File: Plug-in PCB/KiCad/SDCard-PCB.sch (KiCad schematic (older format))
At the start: 0 parts

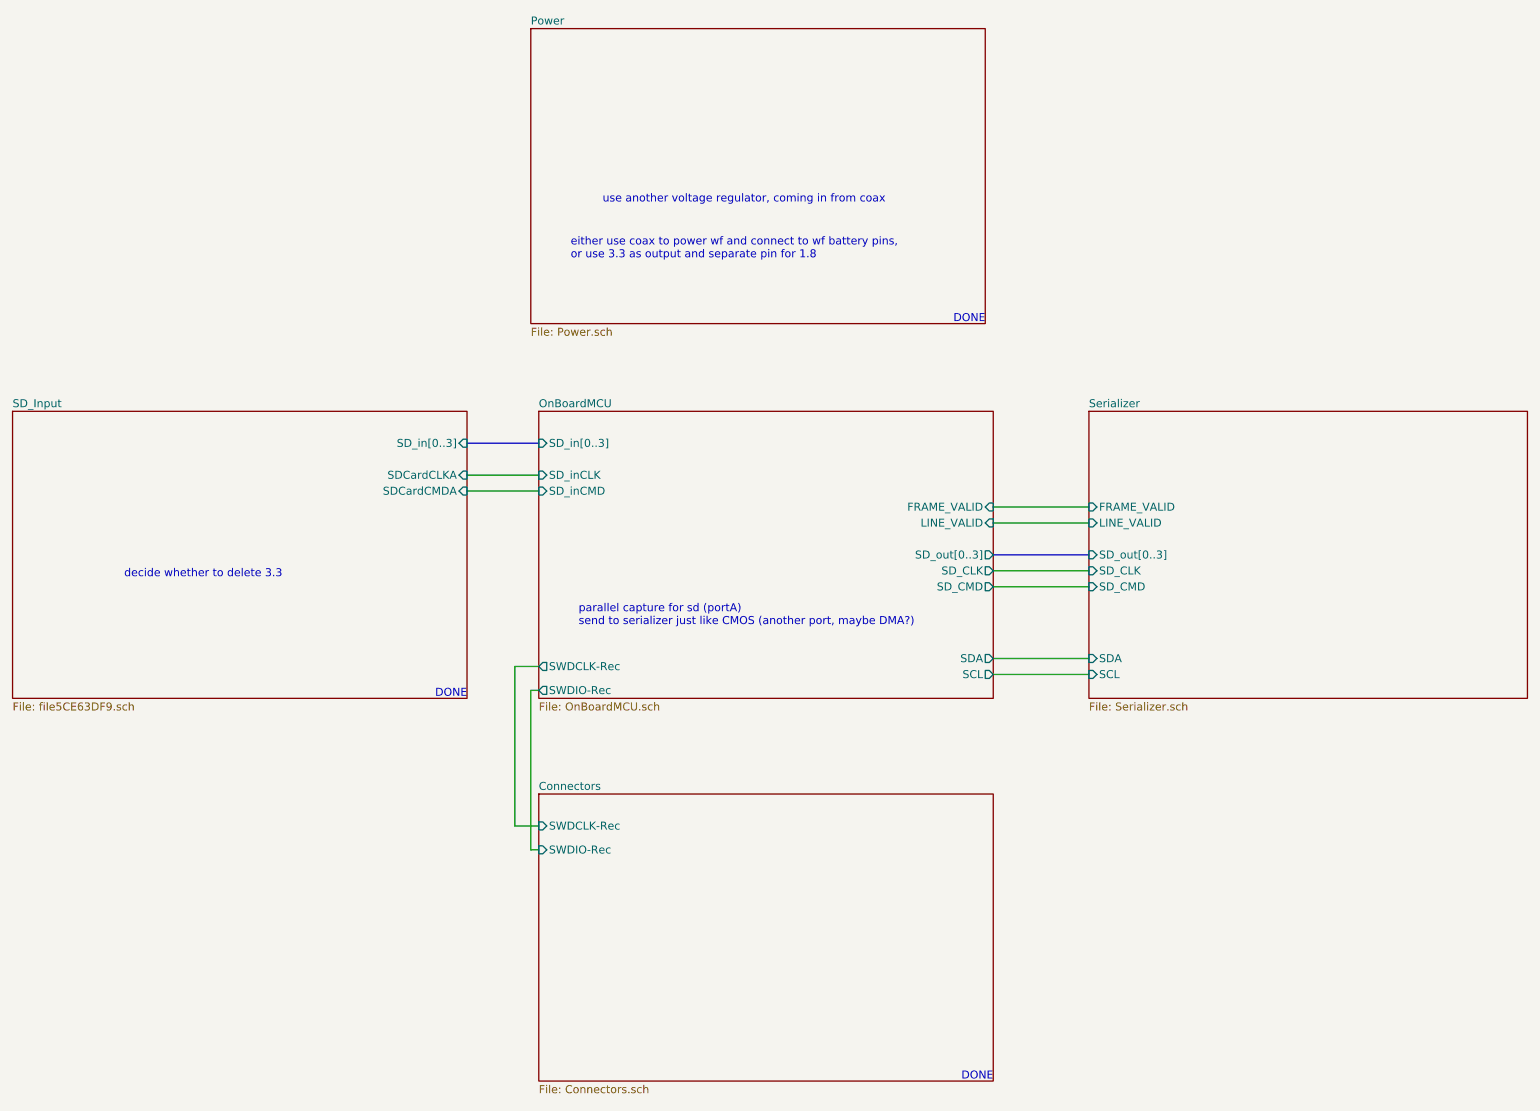
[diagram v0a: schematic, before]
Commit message: Wired Expansion Board Update
1. Begin hardcoding bit-bang communication between wirefree MCU and wired expansion MCU.
++ Can I use the PIO module on the pins to send data in sync while grabbing image from the sensor with parallel capture mode?

2. Wired expansion board schematics and layout modifications
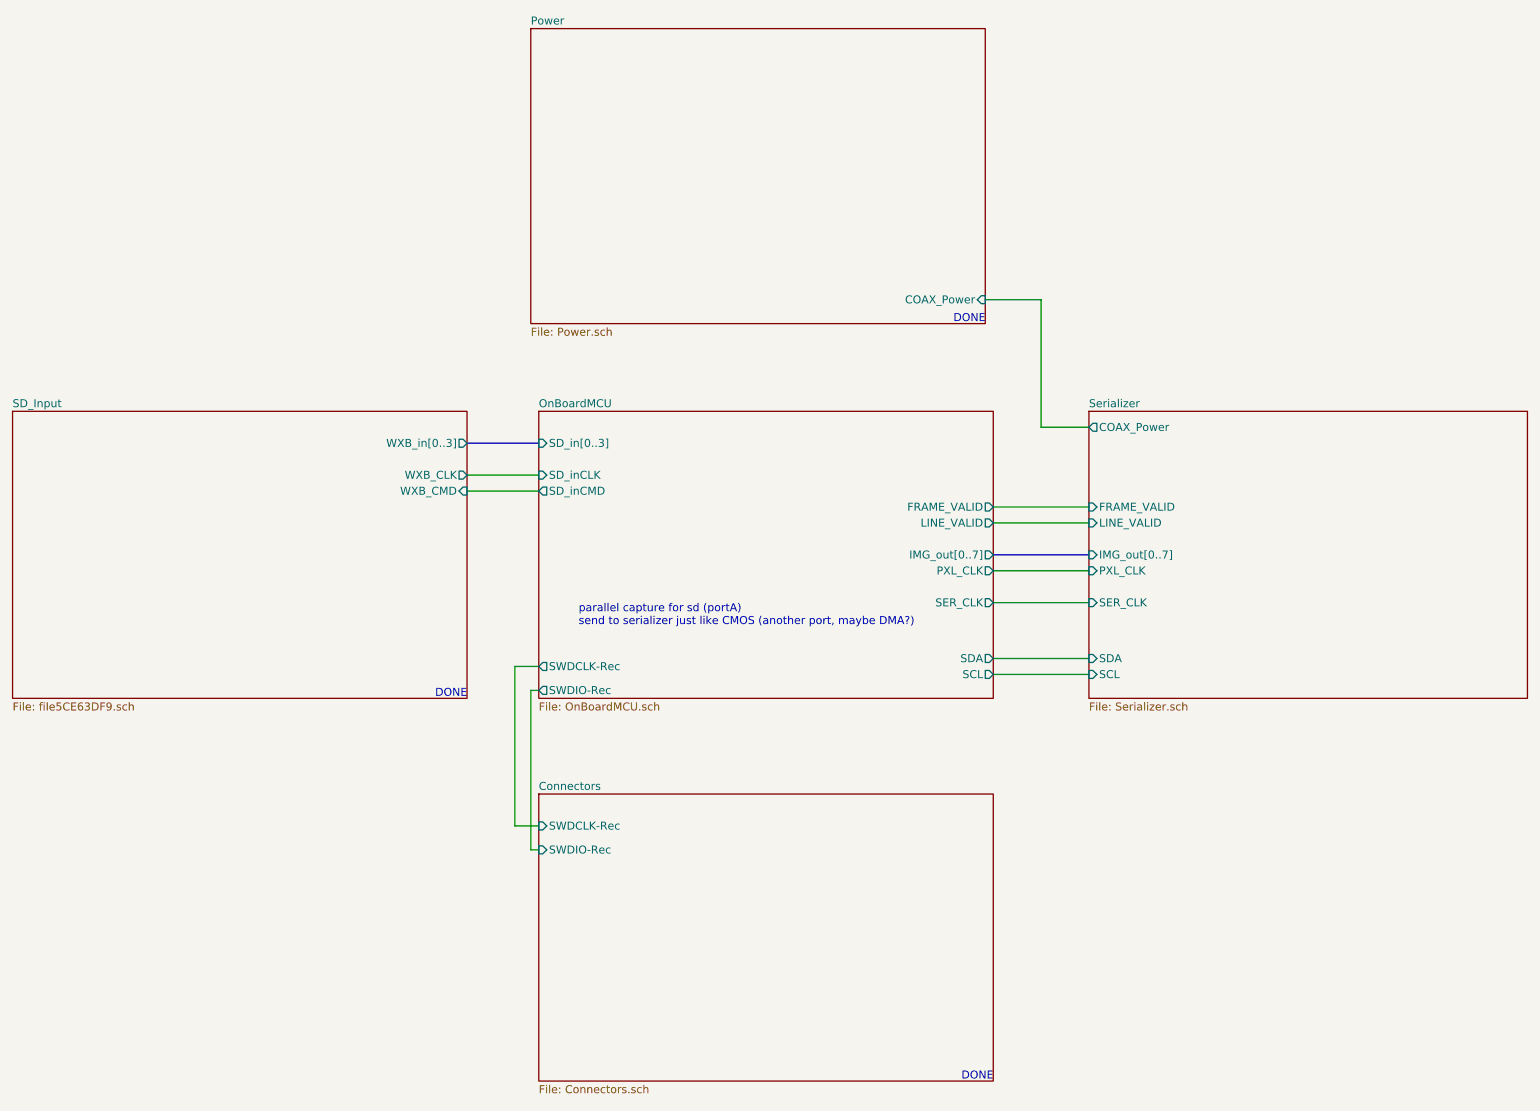
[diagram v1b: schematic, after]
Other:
- note removed: "decide whether to delete 3.3"
- note removed: "either use coax to power wf and connect to wf battery pins, \nor use 3.3 as output and separate pin for 1.8"
- note removed: "use another voltage regulator, coming in from coax"
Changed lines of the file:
@@
 F2 "FRAME_VALID" I L 7600 4050 50
 F3 "LINE_VALID" I L 7600 4150 50
-F4 "SD_out[0..3]" I L 7600 4350 50
-F5 "SD_CMD" I L 7600 4550 50
-F6 "SD_CLK" I L 7600 4450 50
-F7 "SDA" I L 7600 5000 50
-F8 "SCL" I L 7600 5100 50
+F4 "SDA" I L 7600 5000 50
+F5 "SCL" I L 7600 5100 50
+F6 "IMG_out[0..7]" I L 7600 4350 50
+F7 "SER_CLK" I L 7600 4650 50
+F8 "PXL_CLK" I L 7600 4450 50
+F9 "COAX_Power" O L 7600 3550 50
 $EndSheet
 Wire Wire Line
@@
 F0 "Power" 50
 F1 "Power.sch" 50
+F2 "COAX_Power" I R 6950 2750 50
 $EndSheet
 Wire Wire Line
@@
 Wire Wire Line
 	4100 6200 4150 6200
-$Sheet
-S 850  3450 2850 1800
-U 5CE63DFA
-F0 "SD_Input" 50
-F1 "file5CE63DF9.sch" 50
-F2 "SDCardCMDA" I R 3700 3950 50
-F3 "SDCardCLKA" I R 3700 3850 50
-F4 "SD_in[0..3]" I R 3700 3650 50
-$EndSheet
-Wire Wire Line
-	3700 3950 4150 3950
 Wire Wire Line
 	4150 3850 3700 3850
@@
 Wire Bus Line
 	3700 3650 4150 3650
-$Sheet
-S 4150 3450 2850 1800
-U 5CC244CB
-F0 "OnBoardMCU" 50
-F1 "OnBoardMCU.sch" 50
-F2 "SWDIO-Rec" O L 4150 5200 50
-F3 "SWDCLK-Rec" O L 4150 5050 50
-F4 "SD_out[0..3]" O R 7000 4350 50
-F5 "LINE_VALID" I R 7000 4150 50
-F6 "FRAME_VALID" I R 7000 4050 50
-F7 "SD_in[0..3]" I L 4150 3650 50
-F8 "SD_inCLK" I L 4150 3850 50
-F9 "SD_inCMD" I L 4150 3950 50
-F10 "SD_CLK" O R 7000 4450 50
-F11 "SD_CMD" O R 7000 4550 50
-F12 "SDA" O R 7000 5000 50
-F13 "SCL" O R 7000 5100 50
-$EndSheet
 Wire Bus Line
 	7000 4350 7600 4350
 Wire Wire Line
 	7000 4450 7600 4450
-Wire Wire Line
-	7000 4550 7600 4550
 Wire Wire Line
 	7000 4050 7600 4050
@@
 Wire Wire Line
 	7000 5100 7600 5100
-Text Notes 4350 2500 0    50   ~ 0
-either use coax to power wf and connect to wf battery pins, \nor use 3.3 as output and separate pin for 1.8
-Text Notes 1550 4500 0    50   ~ 0
-decide whether to delete 3.3
 Text Notes 4400 4800 0    50   ~ 0
 parallel capture for sd (portA)\nsend to serializer just like CMOS (another port, maybe DMA?)
-Text Notes 4550 2150 0    50   ~ 0
-use another voltage regulator, coming in from coax
+Wire Wire Line
+	7000 4650 7600 4650
+Wire Wire Line
+	7600 3550 7300 3550
+Wire Wire Line
+	7300 3550 7300 2750
+Wire Wire Line
+	7300 2750 6950 2750
+Wire Wire Line
+	3700 3950 4150 3950
+$Sheet
+S 4150 3450 2850 1800
+U 5CC244CB
+F0 "OnBoardMCU" 50
+F1 "OnBoardMCU.sch" 50
+F2 "SWDIO-Rec" O L 4150 5200 50
+F3 "SWDCLK-Rec" O L 4150 5050 50
+F4 "SD_in[0..3]" I L 4150 3650 50
+F5 "SD_inCLK" I L 4150 3850 50
+F6 "SDA" O R 7000 5000 50
+F7 "SCL" O R 7000 5100 50
+F8 "SER_CLK" O R 7000 4650 50
+F9 "LINE_VALID" O R 7000 4150 50
+F10 "FRAME_VALID" O R 7000 4050 50
+F11 "IMG_out[0..7]" O R 7000 4350 50
+F12 "PXL_CLK" O R 7000 4450 50
+F13 "SD_inCMD" O L 4150 3950 50
+$EndSheet
+$Sheet
+S 850  3450 2850 1800
+U 5CE63DFA
+F0 "SD_Input" 50
+F1 "file5CE63DF9.sch" 50
+F2 "WXB_CLK" O R 3700 3850 50
+F3 "WXB_in[0..3]" O R 3700 3650 50
+F4 "WXB_CMD" I R 3700 3950 50
+$EndSheet
 $EndSCHEMATC

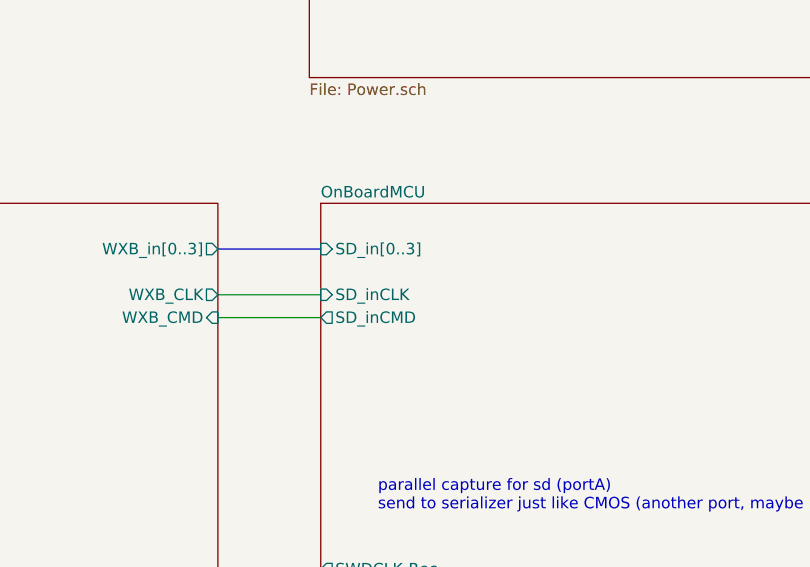
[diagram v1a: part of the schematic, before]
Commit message: Wired Expansion Board Updates
1. KiCad: Schematics and layouts completed/Gerber files generated
2. Atmel: Communication protocol from WireFree to WiredExpansion written
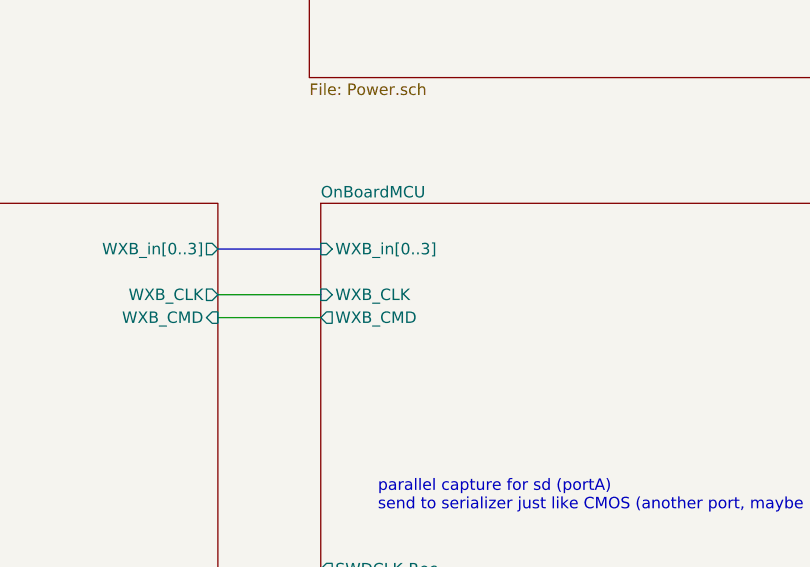
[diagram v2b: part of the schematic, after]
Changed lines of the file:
@@
 	3700 3950 4150 3950
-$Sheet
-S 4150 3450 2850 1800
-U 5CC244CB
-F0 "OnBoardMCU" 50
-F1 "OnBoardMCU.sch" 50
-F2 "SWDIO-Rec" O L 4150 5200 50
-F3 "SWDCLK-Rec" O L 4150 5050 50
-F4 "SD_in[0..3]" I L 4150 3650 50
-F5 "SD_inCLK" I L 4150 3850 50
-F6 "SDA" O R 7000 5000 50
-F7 "SCL" O R 7000 5100 50
-F8 "SER_CLK" O R 7000 4650 50
-F9 "LINE_VALID" O R 7000 4150 50
-F10 "FRAME_VALID" O R 7000 4050 50
-F11 "IMG_out[0..7]" O R 7000 4350 50
-F12 "PXL_CLK" O R 7000 4450 50
-F13 "SD_inCMD" O L 4150 3950 50
-$EndSheet
 $Sheet
 S 850  3450 2850 1800
@@
 F4 "WXB_CMD" I R 3700 3950 50
 $EndSheet
+$Sheet
+S 4150 3450 2850 1800
+U 5CC244CB
+F0 "OnBoardMCU" 50
+F1 "OnBoardMCU.sch" 50
+F2 "SWDIO-Rec" O L 4150 5200 50
+F3 "SWDCLK-Rec" O L 4150 5050 50
+F4 "WXB_in[0..3]" I L 4150 3650 50
+F5 "WXB_CLK" I L 4150 3850 50
+F6 "SDA" O R 7000 5000 50
+F7 "SCL" O R 7000 5100 50
+F8 "SER_CLK" O R 7000 4650 50
+F9 "LINE_VALID" O R 7000 4150 50
+F10 "FRAME_VALID" O R 7000 4050 50
+F11 "IMG_out[0..7]" O R 7000 4350 50
+F12 "PXL_CLK" O R 7000 4450 50
+F13 "WXB_CMD" O L 4150 3950 50
+$EndSheet
 $EndSCHEMATC
